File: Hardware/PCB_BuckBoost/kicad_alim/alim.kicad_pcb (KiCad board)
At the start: 2 copper layers, 58.4 x 58.4 mm, 36 parts, among them J1 Conn_01x02, J2 Conn_01x02, J3 Conn_01x02, J4 Conn_01x02, U1 MIC3172YM, U2 MIC3172YM

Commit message: routage Buck quasi terminé
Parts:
- moved L1 6.60 mm to (185.9, 93.7)
- moved D3 4.69 mm to (189.5, 87.9), turned to -90 degrees
- moved R3 2.65 mm to (187.7, 87.9), turned to 90 degrees
- moved R1 1.52 mm to (178.2, 88.9), turned to 0 degrees
- moved R4 1.52 mm to (188.5, 90.4)
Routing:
- net Net-(D2-K): track 0.00 -> 26.9 mm, vias 0 -> 4
- net +5V: track 0.00 -> 15.2 mm
- net Net-(U1-FB): track 0.00 -> 15.1 mm, vias 0 -> 2
- net Net-(D1-K): track 0.00 -> 11.2 mm
- net +15V: track 0.00 -> 9.29 mm, vias 0 -> 2
- net Net-(U1-COMP): track 0.00 -> 6.58 mm
- net GND: track 0.00 -> 5.70 mm
- net Net-(D3-K): track 0.00 -> 4.52 mm
- net Net-(C4-Pad1): track 0.00 -> 2.34 mm
- net Net-(D3-A): track 0.00 -> 1.48 mm

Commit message: PCB BUCK/BOOST
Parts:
- moved PS1 152.5 mm to (196.6, 90.8), turned to 90 degrees
- moved D5 127.9 mm to (194.6, 92.9)
- moved C5 126.3 mm to (194.8, 94.6), turned to 180 degrees
- moved C1 118.6 mm to (191.3, 92.9)
- moved R8 115.6 mm to (195.5, 90.2), turned to -90 degrees
- moved C8 42.4 mm to (193.1, 97.5), turned to 90 degrees
- moved R7 38.1 mm to (193.1, 101.1), turned to -90 degrees
- moved R5 35.9 mm to (191.5, 97.5), turned to 90 degrees
- moved R6 35.5 mm to (191.5, 101.0), turned to 90 degrees
- moved L2 25.2 mm to (181.9, 99.1), turned to -90 degrees
- moved U2 23.7 mm to (186.9, 99.8), turned to 180 degrees
- moved H3 20.4 mm to (171.9, 118.9)
- moved H1 20.4 mm to (171.9, 69.3)
- moved J3 20.4 mm to (173.4, 93.7)
- moved C9 18.5 mm to (193.3, 108.4), turned to 0 degrees
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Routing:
- net +15V: track 9.29 -> 73.2 mm, vias 2 -> 6
- net GND: track 5.70 -> 57.3 mm, vias 0 -> 6
- net +3.3V: track 0.00 -> 47.4 mm, vias 0 -> 2
- net +5V: track 15.2 -> 50.4 mm
- net Routeur: track 0.00 -> 18.8 mm
- net Net-(U2-COMP): track 0.00 -> 8.80 mm
- net Net-(D4-A): track 0.00 -> 7.34 mm
- net Net-(U2-FB): track 0.00 -> 4.12 mm
- net Net-(D5-A): track 0.00 -> 1.88 mm
- net Net-(C8-Pad2): track 0.00 -> 1.59 mm
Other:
- board size 58.4 x 58.4 mm -> 38 x 57.3 mm
- board text added: "BOOST"
- board text added: "BUCK"
- board text added: "COHOMA_BALISE"

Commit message: PCB Final en avancement
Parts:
- PS1: footprint Custom_BUCKBOOST:ssop5 (copy) -> Package_TO_SOT_SMD:TSOT-23-5_HandSoldering
- moved L2 65.3 mm to (116.8, 105.0)
- moved R8 61.7 mm to (134.1, 96.2)
- moved C10 61.1 mm to (121.3, 119.4)
- moved D4 60.7 mm to (125.7, 109.5)
- moved R5 60.7 mm to (131.7, 108.1)
- moved R7 60.7 mm to (133.3, 111.7)
- moved D5 59.1 mm to (135.5, 91.6)
- moved R6 55.3 mm to (138.0, 114.9)
- moved C8 54.8 mm to (139.7, 109.9)
- moved C7 38.5 mm to (163.6, 104.6)
- moved J3 24.0 mm to (193.3, 107.2), turned to 90 degrees
- moved C2 20.9 mm to (166.6, 90.2)
- moved J1 20.2 mm to (193.3, 87.7), turned to 90 degrees
- moved D2 18.4 mm to (169.2, 91.5)
- moved C5 15.2 mm to (185.4, 82.7)
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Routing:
- net +15V: track 73.2 -> 0.00 mm
- net GND: track 57.3 -> 0.00 mm
- net +5V: track 50.4 -> 0.00 mm
- net +3.3V: track 47.4 -> 0.00 mm
- net Net-(D2-K): track 26.9 -> 0.00 mm
- net Routeur: track 18.8 -> 0.00 mm
- net Net-(U1-FB): track 15.1 -> 0.00 mm
- net Net-(D1-K): track 11.2 -> 0.00 mm
- net Net-(U2-COMP): track 8.80 -> 0.00 mm
- net Net-(D4-A): track 7.34 -> 0.00 mm
- net Net-(U1-COMP): track 6.58 -> 0.00 mm
- net Net-(D3-K): track 4.52 -> 0.00 mm
- net Net-(U2-FB): track 4.12 -> 0.00 mm
- net Net-(C4-Pad1): track 2.34 -> 0.00 mm
- net Net-(D5-A): track 1.88 -> 0.00 mm
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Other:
- board outline removed

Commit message: oui
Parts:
- moved R8 51.3 mm to (183.9, 108.5), turned to 0 degrees
- moved R7 50.8 mm to (183.9, 107.0), turned to 180 degrees
- moved R6 46.9 mm to (183.9, 105.5), turned to 180 degrees
- moved C8 44.3 mm to (184.0, 110.1), turned to 180 degrees
- moved R5 39.6 mm to (171.3, 108.4), turned to 180 degrees
- moved C9 0.44 mm to (180.4, 116.4)
- turned U2 to 0 degrees
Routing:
- net Net-(U1-FB): vias 2 -> 0
- net Net-(D2-K): vias 4 -> 0
- net +15V: vias 6 -> 3

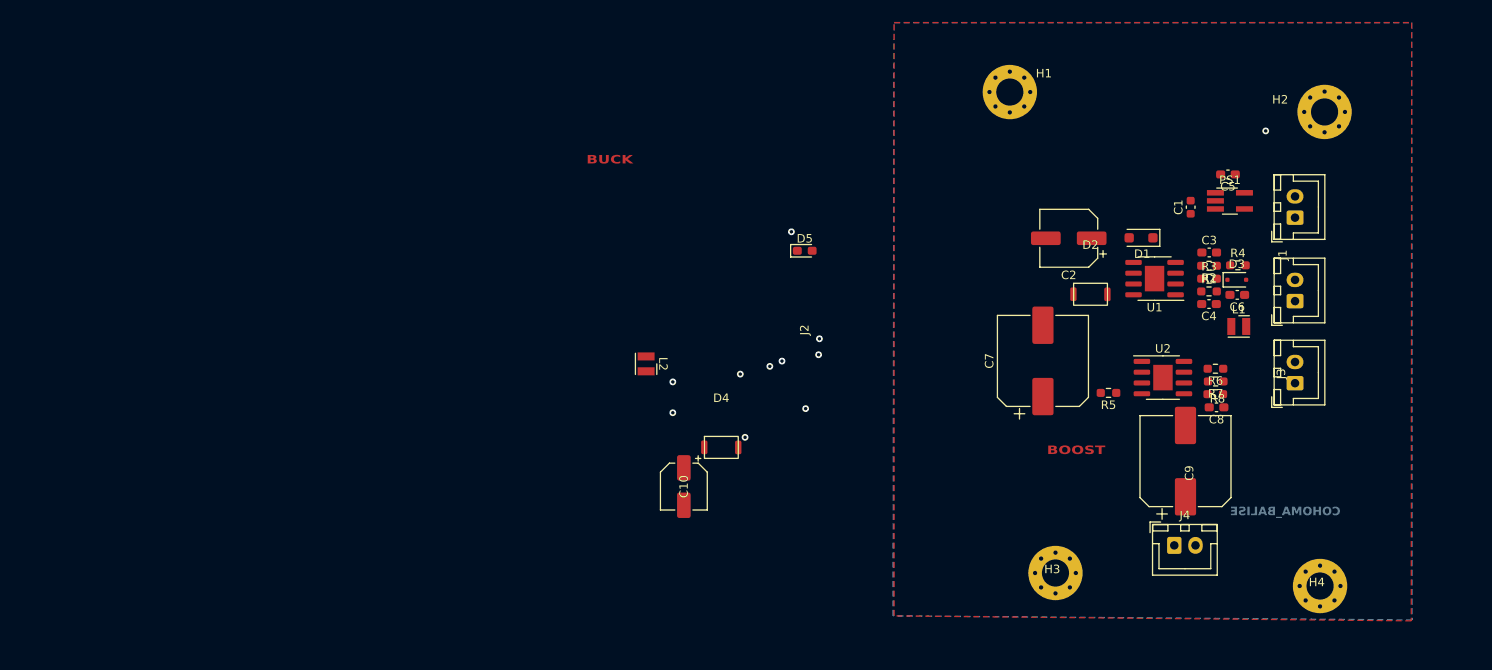
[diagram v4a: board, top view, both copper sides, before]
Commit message: PCB presque fini (manque les liaisons)
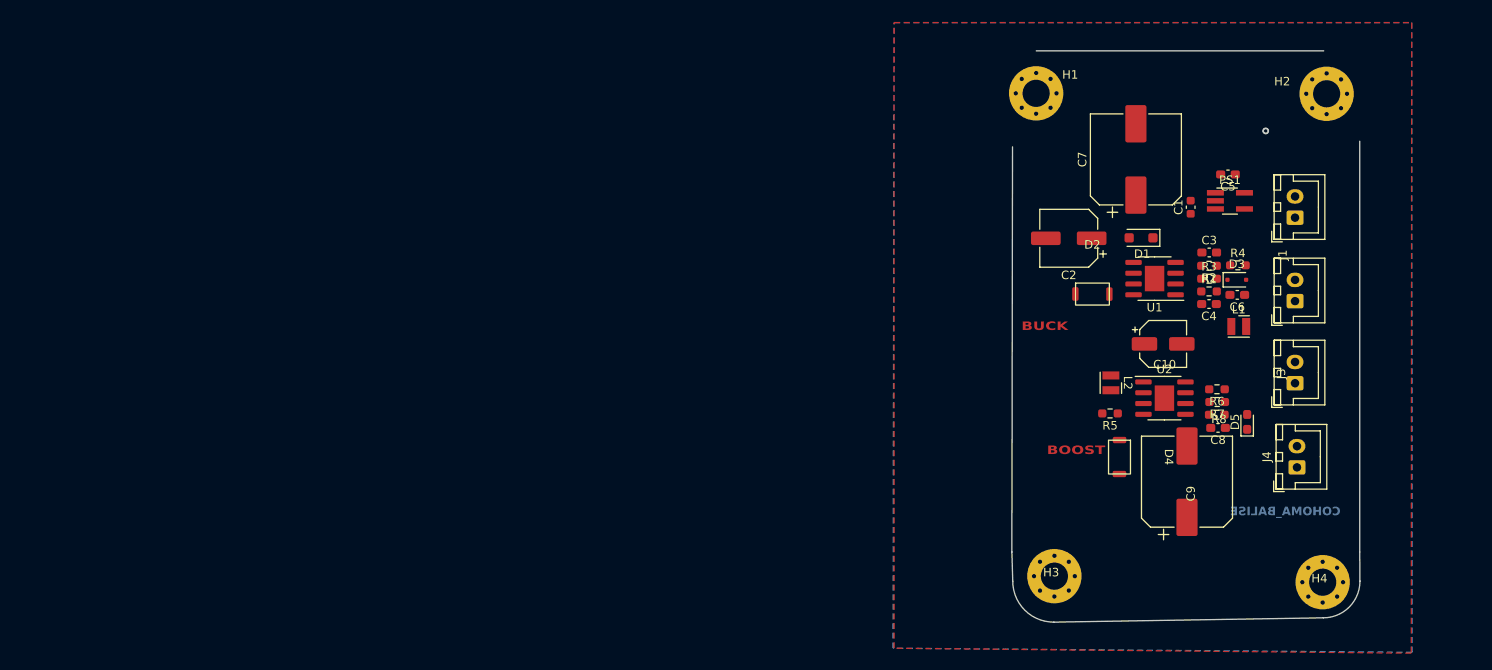
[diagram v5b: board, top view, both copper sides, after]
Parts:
- moved C10 58.9 mm to (177.7, 102.6), turned to 0 degrees
- moved D5 55.9 mm to (187.6, 111.8), turned to 90 degrees
- moved L2 54.8 mm to (171.6, 107.2)
- moved D4 52.6 mm to (177.9, 115.9), turned to -90 degrees
- moved C7 26.1 mm to (174.5, 80.9)
- moved J4 17.1 mm to (193.5, 117.2), turned to 90 degrees
- moved H1 3.10 mm to (162.8, 73.1)
- moved C8 2.43 mm to (184.2, 112.5)
- moved C9 2.43 mm to (180.5, 118.8)
- moved R5 2.43 mm to (171.5, 110.8)
- moved R6 2.43 mm to (184.1, 108.0)
- moved U2 2.43 mm to (177.9, 109.0)
- moved R7 2.43 mm to (184.1, 109.5)
- moved R8 2.43 mm to (184.1, 111.0)
- moved H2 2.15 mm to (197.0, 73.2)
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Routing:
- net GND: vias 6 -> 0
- net +3.3V: vias 2 -> 1
- net +15V: vias 3 -> 0
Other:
- board outline added: 41 x 67.3 mm

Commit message: a
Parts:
- moved H4 3.36 mm to (197.2, 127.4)
- moved H3 2.82 mm to (164.0, 127.3)
- moved H1 1.33 mm to (164.0, 73.6)
- moved H2 0.54 mm to (197.3, 73.6)
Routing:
- net Routeur: track 0.00 -> 38.6 mm, vias 0 -> 2
- net +15V: track 0.00 -> 37.8 mm, vias 0 -> 1
- net Net-(D2-K): track 0.00 -> 33.4 mm, vias 0 -> 4
- net +5V: track 0.00 -> 32.4 mm
- net Net-(C8-Pad2): track 0.00 -> 25.4 mm, vias 0 -> 2
- net Net-(U2-FB): track 0.00 -> 16.2 mm, vias 0 -> 2
- net Net-(D1-K): track 0.00 -> 12.5 mm
- net +3.3V: track 0.00 -> 8.75 mm, vias 1 -> 0
- net Net-(D4-A): track 0.00 -> 6.29 mm
- net Net-(U1-FB): track 0.00 -> 5.75 mm
- net Net-(D3-K): track 0.00 -> 4.07 mm
- net Net-(U2-COMP): track 0.00 -> 4.03 mm
- net Net-(U1-COMP): track 0.00 -> 3.39 mm
- net Net-(D5-A): track 0.00 -> 2.68 mm
- net Net-(D3-A): track 0.00 -> 2.58 mm
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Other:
- board size 41 x 67.3 mm -> 43.7 x 63.9 mm

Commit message: pcb v1 buck boost
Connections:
- R1 pad 1: Net-(U1-COMP) -> Net-(D2-K)
- U1 pad 2: Net-(U1-COMP) -> Net-(D2-K)
- U1 pad 9: (no net) -> Net-(D2-K)
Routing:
- net +15V: track 37.8 -> 66.7 mm, vias 1 -> 3
- net +5V: track 32.4 -> 47.2 mm
- net Net-(D4-A): track 6.29 -> 13.3 mm
- net Net-(D2-K): track 33.4 -> 36.8 mm
- net Net-(U1-COMP): track 3.39 -> 0.00 mm
